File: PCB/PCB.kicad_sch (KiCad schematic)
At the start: 5 parts, among them J1 Ultrasonic Sensor, U1 Buck Converter Module, U2 Buck Converter Module, U3 ESP32-WROOM-32

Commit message: PCB Version
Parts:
- removed J1: Ultrasonic Sensor, Connector_PinHeader_2.54mm:PinHeader_1x04_P2.54mm_Vertical, symbol Connector:Conn_01x04_Socket
- U2: value Buck Converter Module -> Ultrasonic Sensor
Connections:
- net +5V: now reaches U2.1 (Pin_1)
- net Trig: now reaches U2.2 (Pin_2)
- net Trig: now also U3.26 (IO4)
- net Echo: now reaches U2.3 (Pin_3)
- net Echo: now also U3.29 (IO5)
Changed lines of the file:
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@@
+	(wire
+		(pts
+			(xy 106.68 66.04) (xy 104.14 66.04)
+		)
+		(stroke
+			(width 0)
+			(type default)
+		)
+	)
 	(wire
 		(pts
@@
 	(wire
 		(pts
-			(xy 157.48 62.23) (xy 162.56 62.23)
-		)
-		(stroke
-			(width 0)
-			(type default)
-		)
-	)
-	(wire
-		(pts
 			(xy 41.91 46.99) (xy 88.9 46.99)
 		)
@@
 	(wire
 		(pts
-			(xy 157.48 57.15) (xy 157.48 62.23)
-		)
-		(stroke
-			(width 0)
-			(type default)
-		)
-	)
-	(wire
-		(pts
 			(xy 20.32 82.55) (xy 41.91 82.55)
 		)
@@
 	(wire
 		(pts
-			(xy 160.02 59.69) (xy 162.56 59.69)
-		)
-		(stroke
-			(width 0)
-			(type default)
-		)
-	)
-	(wire
-		(pts
 			(xy 41.91 85.09) (xy 38.1 85.09)
 		)
@@
 	(wire
 		(pts
-			(xy 160.02 54.61) (xy 160.02 59.69)
+			(xy 123.19 64.77) (xy 123.19 58.42)
+		)
+		(stroke
+			(width 0)
+			(type default)
+		)
+	)
+	(wire
+		(pts
+			(xy 107.95 63.5) (xy 104.14 63.5)
+		)
+		(stroke
+			(width 0)
+			(type default)
+		)
+	)
+	(wire
+		(pts
+			(xy 125.73 67.31) (xy 107.95 67.31)
+		)
+		(stroke
+			(width 0)
+			(type default)
+		)
+	)
+	(wire
+		(pts
+			(xy 107.95 67.31) (xy 107.95 63.5)
 		)
 		(stroke
@@
 	(wire
 		(pts
-			(xy 142.24 54.61) (xy 160.02 54.61)
+			(xy 106.68 69.85) (xy 106.68 66.04)
+		)
+		(stroke
+			(width 0)
+			(type default)
+		)
+	)
+	(wire
+		(pts
+			(xy 125.73 64.77) (xy 123.19 64.77)
+		)
+		(stroke
+			(width 0)
+			(type default)
+		)
+	)
+	(wire
+		(pts
+			(xy 125.73 69.85) (xy 106.68 69.85)
 		)
 		(stroke
@@
 		)
 	)
-	(wire
-		(pts
-			(xy 142.24 57.15) (xy 157.48 57.15)
-		)
-		(stroke
-			(width 0)
-			(type default)
+	(label "Echo"
+		(at 118.11 69.85 0)
+		(effects
+			(font
+				(size 1.27 1.27)
+			)
+			(justify left bottom)
 		)
 	)
 	(label "3V3"
 		(at 85.09 46.99 0)
+		(effects
+			(font
+				(size 1.27 1.27)
+			)
+			(justify left bottom)
+		)
+	)
+	(label "Trig"
+		(at 118.11 67.31 0)
 		(effects
 			(font
@@
 	)
 	(symbol
+		(lib_id "power:+5V")
+		(at 123.19 58.42 0)
+		(unit 1)
+		(body_style 1)
+		(exclude_from_sim no)
+		(in_bom yes)
+		(on_board yes)
+		(in_pos_files yes)
+		(dnp no)
+		(fields_autoplaced yes)
+		(property "Reference" "#PWR05"
+			(at 123.19 62.23 0)
+			(hide yes)
+			(show_name no)
+			(do_not_autoplace no)
+			(effects
+				(font
+					(size 1.27 1.27)
+				)
+			)
+		)
+		(property "Value" "+5V"
+			(at 123.19 53.34 0)
+			(show_name no)
+			(do_not_autoplace no)
+			(effects
+				(font
+					(size 1.27 1.27)
+				)
+			)
+		)
+		(property "Footprint" ""
+			(at 123.19 58.42 0)
+			(hide yes)
+			(show_name no)
+			(do_not_autoplace no)
+			(effects
+				(font
+					(size 1.27 1.27)
+				)
+			)
+		)
+		(property "Datasheet" ""
+			(at 123.19 58.42 0)
+			(hide yes)
+			(show_name no)
+			(do_not_autoplace no)
+			(effects
+				(font
+					(size 1.27 1.27)
+				)
+			)
+		)
+		(property "Description" "Power symbol creates a global label with name \"+5V\""
+			(at 123.19 58.42 0)
+			(hide yes)
+			(show_name no)
+			(do_not_autoplace no)
+			(effects
+				(font
+					(size 1.27 1.27)
+				)
+			)
+		)
+		(pin "1"
+		)
+		(instances
+			(project "PCB"
+				(path "/ab40fc32-b885-4754-9572-45a5defa6a02"
+					(reference "#PWR05")
+					(unit 1)
+				)
+			)
+		)
+	)
+	(symbol
 		(lib_id "power:GND")
 		(at 88.9 119.38 0)
@@
 			)
 		)
-		(property "Value" "Buck Converter Module"
+		(property "Value" "Ultrasonic Sensor"
 			(at 133.35 69.8499 0)
 			(show_name no)
@@
 					(unit 1)
 				)
-			)
-		)
-	)
-	(symbol
-		(lib_id "Connector:Conn_01x04_Socket")
-		(at 167.64 59.69 0)
-		(unit 1)
-		(body_style 1)
-		(exclude_from_sim no)
-		(in_bom yes)
-		(on_board yes)
-		(in_pos_files yes)
-		(dnp no)
-		(property "Reference" "J1"
-			(at 171.958 61.976 0)
-			(hide yes)
-			(show_name no)
-			(do_not_autoplace no)
-			(effects
-				(font
-					(size 1.27 1.27)
-				)
-				(justify left)
-			)
-		)
-		(property "Value" "Ultrasonic Sensor"
-			(at 168.148 61.214 0)
-			(show_name no)
-			(do_not_autoplace no)
-			(effects
-				(font
-					(size 1.27 1.27)
-				)
-				(justify left)
-			)
-		)
-		(property "Footprint" "Connector_PinHeader_2.54mm:PinHeader_1x04_P2.54mm_Vertical"
-			(at 167.64 59.69 0)
-			(hide yes)
-			(show_name no)
-			(do_not_autoplace no)
-			(effects
-				(font
-					(size 1.27 1.27)
-				)
-			)
-		)
-		(property "Datasheet" ""
-			(at 167.64 59.69 0)
-			(hide yes)
-			(show_name no)
-			(do_not_autoplace no)
-			(effects
-				(font
-					(size 1.27 1.27)
-				)
-			)
-		)
-		(property "Description" "Generic connector, single row, 01x04, script generated"
-			(at 167.64 59.69 0)
-			(hide yes)
-			(show_name no)
-			(do_not_autoplace no)
-			(effects
-				(font
-					(size 1.27 1.27)
-				)
-			)
-		)
-		(pin "2"
-		)
-		(pin "4"
-		)
-		(pin "3"
-		)
-		(pin "1"
-		)
-		(instances
-			(project "PCB"
-				(path "/ab40fc32-b885-4754-9572-45a5defa6a02"
-					(reference "J1")
-					(unit 1)
-				)

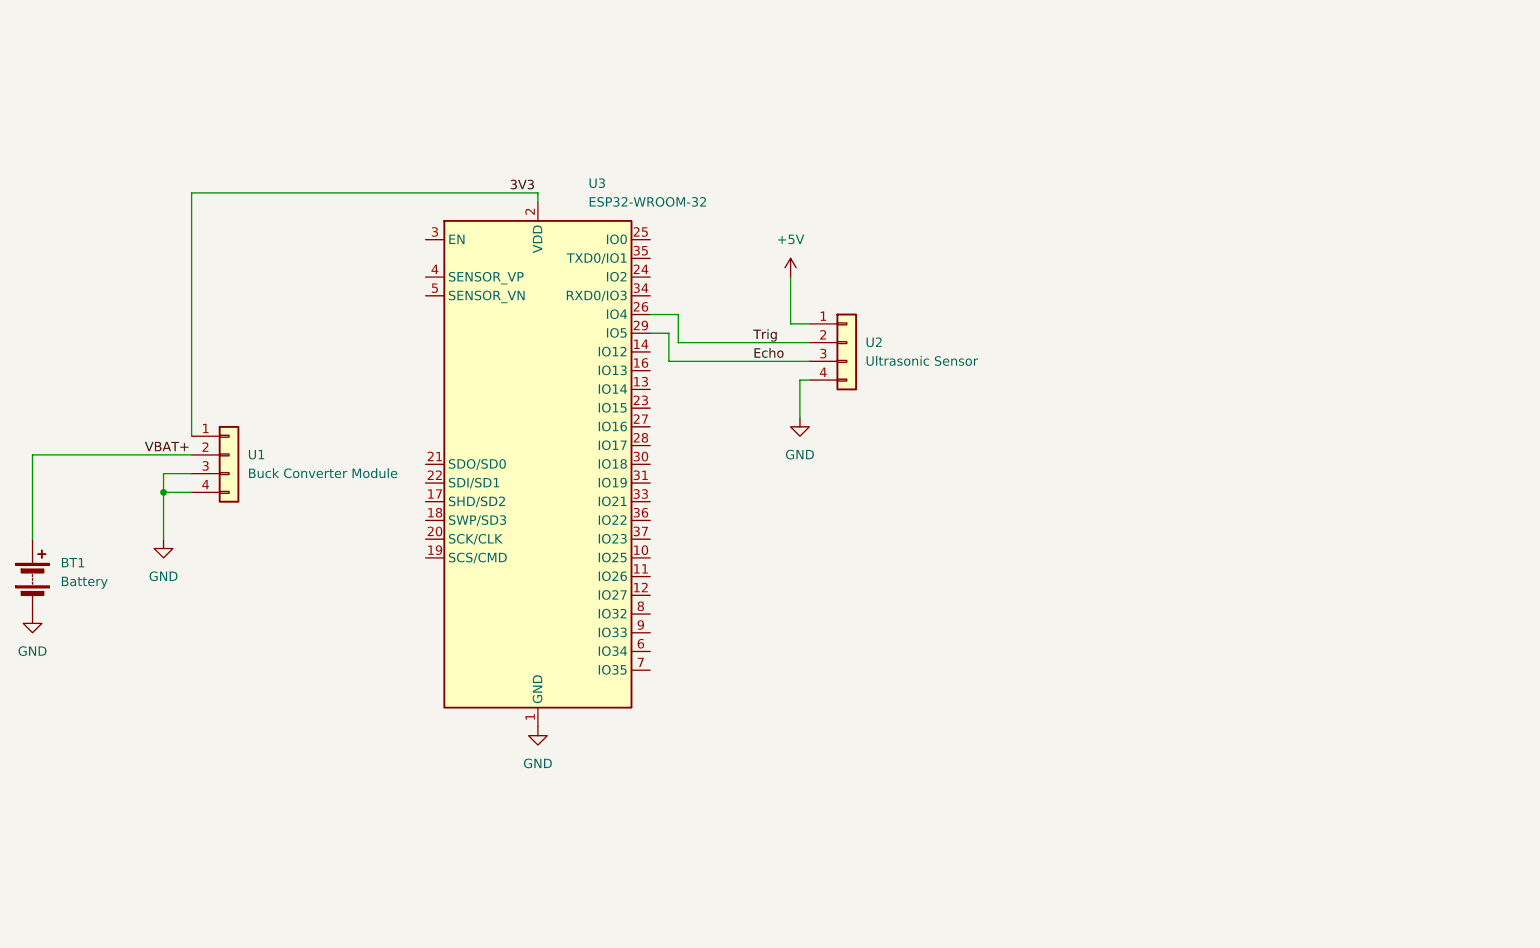
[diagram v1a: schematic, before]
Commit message: Update the PCB to support the new 4S batteyr charger, cleaned up the diagram, and added battery indicator support
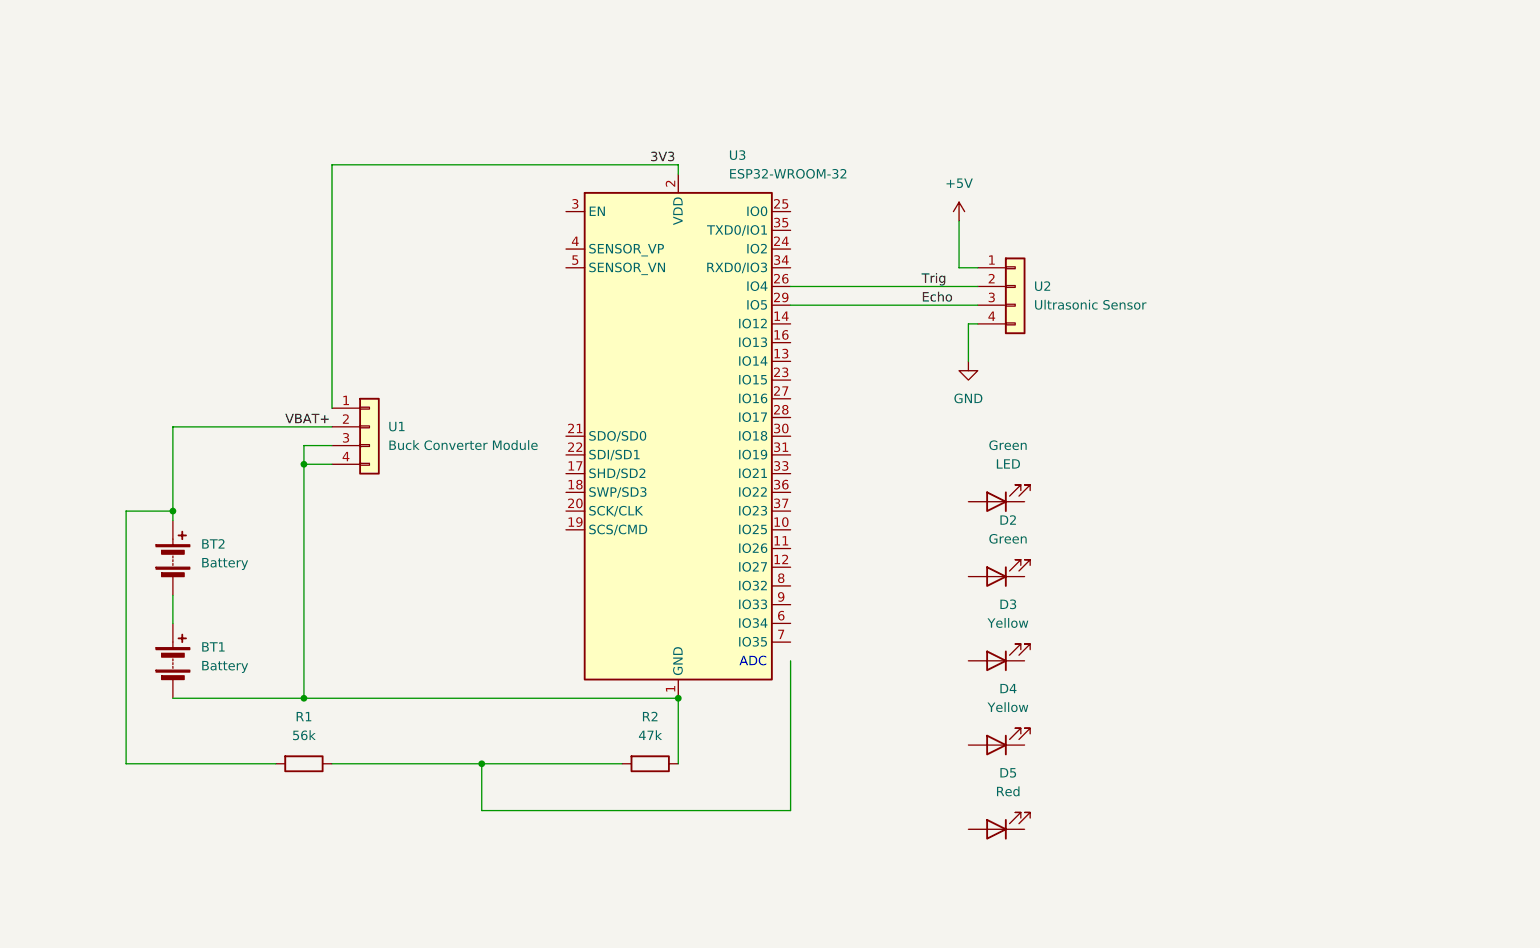
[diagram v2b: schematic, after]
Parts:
- added BT2: Battery, Battery:BatteryHolder_Keystone_2462_2xAA, symbol Device:Battery
- added D2: Green, symbol Device:LED
- added D3, D4: Yellow, symbol Device:LED
- added D5: Red, symbol Device:LED
- added Green: LED, symbol Device:LED
- added R1: 56k, symbol Device:R
- added R2: 47k, symbol Device:R
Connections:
- net GND: no longer BT1.2 (-), U1.3 (Pin_3), U1.4 (Pin_4), U3.1 (GND), U3.15 (GND), U3.38 (GND), U3.39 (GND)
- net VBAT+: now also BT2.1 (+), R1.2; no longer BT1.1 (+)
- new net: BT1.2 (-), R2.1, U1.3 (Pin_3), U1.4 (Pin_4), U3.1 (GND), U3.15 (GND), U3.38 (GND), U3.39 (GND)
- new net: BT1.1 (+), BT2.2 (-)
- new net: R1.1, R2.2
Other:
- note added: "ADC"
- moved on the sheet: BT1, U1, U2, U3

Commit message: Update PCB.kicad_sch
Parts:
- added J1: NiMH CHARGER CIRCUIT, symbol Connector_Generic:Conn_01x04
- U1: value Buck Converter Module -> Buck Converter
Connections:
- net ESP32-: now reaches R2.1, U1.3 (Pin_3), U1.4 (Pin_4), U3.1 (GND), U3.15 (GND), U3.38 (GND), U3.39 (GND)
- net ESP32-: now also D2.1 (K), D3.1 (K), D4.1 (K), D5.1 (K), Green.1 (K), J1.4 (Pin_4); no longer BT1.2 (-)
- net VBAT+ renamed 4SPACK+
- net 4SPACK+: now also J1.1 (Pin_1); no longer U1.2 (Pin_2)
- new net 4SPACK-: BT1.2 (-), J1.2 (Pin_2)
- new net OUT+: J1.3 (Pin_3), U1.2 (Pin_2)
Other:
- note added: "4S Battery"
- note added: "Battery Indicator"
- note added: "Battery V Detector"
- moved on the sheet: BT1, BT2, D2, D3, D4, D5, Green, R1, R2, U1, U2, U3

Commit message: Update PCB.kicad_sch
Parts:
- removed U3: ESP32-WROOM-32, RF_Module:ESP32-WROOM-32, symbol RF_Module:ESP32-WROOM-32
- added U4: Custom_ESP32_S3_Board, symbol ESP32_S3_Board:Custom_ESP32_S3_Board
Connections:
- net ESP32- is gone; now on net GND: D2.1 (K), D3.1 (K), D4.1 (K), D5.1 (K), Green.1 (K), J1.4 (Pin_4), R2.1, U1.3 (Pin_3), U1.4 (Pin_4)
- net GND: now also U4.25 (GND)
- net GPIO38: now reaches D2.2 (A)
- net GPIO38: now also U4.36 (GPIO38)
- net GPIO37: now reaches D3.2 (A)
- net GPIO37: now also U4.35 (GPIO37)
- net GPIO36: now reaches D4.2 (A)
- net GPIO36: now also U4.34 (GPIO36)
- net ADC: now reaches R1.1, R2.2
- net ADC: now also U4.4 (GPIO5)
- net GPIO35: now reaches D5.2 (A)
- net GPIO35: now also U4.33 (GPIO35)
- net GPIO39: now reaches Green.2 (A)
- net GPIO39: now also U4.37 (GPIO39)
- net 3V3: no longer names the net of U1.1 (Pin_1)
- net 3V3: now also U4.1 (3V3)
- net Echo renamed ECHO
- net ECHO: now also U4.18 (GPIO13)
- net Trig renamed TRIG
- net TRIG: now also U4.5 (GPIO6)
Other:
- note removed: "ADC"
- moved on the sheet: BT1, BT2, D2, D3, D4, D5, Green, J1, R1, R2, U1, U2

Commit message: PCB optimisation
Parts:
- D2, D3, D4, D5: footprint (none) -> LED_THT:LED_D5.0mm
- Green1: renamed from Green; footprint (none) -> LED_THT:LED_D5.0mm
- J1, U1, U2: footprint (none) -> Connector_PinHeader_2.54mm:PinHeader_1x04_P2.54mm_Vertical
- R1, R2: footprint (none) -> Resistor_THT:R_Axial_DIN0207_L6.3mm_D2.5mm_P7.62mm_Horizontal
- U4: footprint (none) -> Custom:ESP32-S3-DevKitC
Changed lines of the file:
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@@
 			)
 		)
-		(property "Footprint" ""
+		(property "Footprint" "Connector_PinHeader_2.54mm:PinHeader_1x04_P2.54mm_Vertical"
 			(at 85.09 49.53 0)
 			(hide yes)
@@
 			)
 		)
-		(property "Footprint" ""
+		(property "Footprint" "LED_THT:LED_D5.0mm"
 			(at 121.92 106.68 0)
 			(hide yes)
@@
 			)
 		)
-		(property "Footprint" ""
+		(property "Footprint" "LED_THT:LED_D5.0mm"
 			(at 121.92 118.11 0)
 			(hide yes)
@@
 			)
 		)
-		(property "Footprint" ""
+		(property "Footprint" "LED_THT:LED_D5.0mm"
 			(at 121.92 129.54 0)
 			(hide yes)
@@
 			)
 		)
-		(property "Footprint" ""
+		(property "Footprint" "Connector_PinHeader_2.54mm:PinHeader_1x04_P2.54mm_Vertical"
 			(at 82.55 130.81 0)
 			(hide yes)
@@
 			)
 		)
-		(property "Footprint" ""
+		(property "Footprint" "Custom:ESP32-S3-DevKitC"
 			(at 124.46 85.09 0)
 			(hide yes)
@@
 			)
 		)
-		(property "Footprint" ""
+		(property "Footprint" "Resistor_THT:R_Axial_DIN0207_L6.3mm_D2.5mm_P7.62mm_Horizontal"
 			(at 166.37 93.472 90)
 			(hide yes)
@@
 			)
 		)
-		(property "Footprint" ""
+		(property "Footprint" "Resistor_THT:R_Axial_DIN0207_L6.3mm_D2.5mm_P7.62mm_Horizontal"
 			(at 176.53 93.472 90)
 			(hide yes)
@@
 			)
 		)
-		(property "Footprint" ""
+		(property "Footprint" "LED_THT:LED_D5.0mm"
 			(at 121.92 140.97 0)
 			(hide yes)
@@
 		(dnp no)
 		(fields_autoplaced yes)
-		(property "Reference" "Green"
+		(property "Reference" "Green1"
 			(at 123.5075 88.9 0)
 			(show_name no)
@@
 			)
 		)
-		(property "Footprint" ""
+		(property "Footprint" "LED_THT:LED_D5.0mm"
 			(at 121.92 96.52 0)
 			(hide yes)
@@
 			(project "PCB"
 				(path "/ab40fc32-b885-4754-9572-45a5defa6a02"
-					(reference "Green")
+					(reference "Green1")
 					(unit 1)
 				)
@@
 			)
 		)
-		(property "Footprint" ""
+		(property "Footprint" "Connector_PinHeader_2.54mm:PinHeader_1x04_P2.54mm_Vertical"
 			(at 53.34 46.99 0)
 			(hide yes)

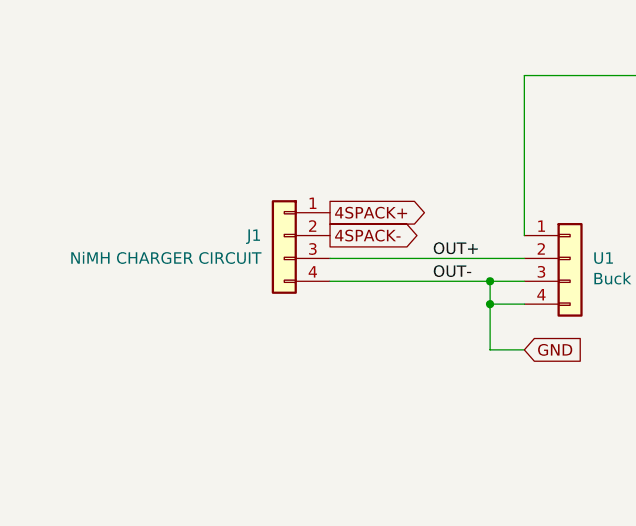
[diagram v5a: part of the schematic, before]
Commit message: removed unused component
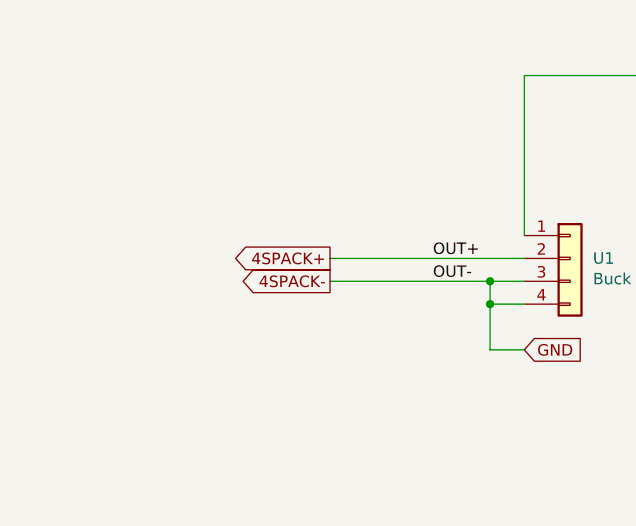
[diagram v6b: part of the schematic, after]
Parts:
- removed J1: NiMH CHARGER CIRCUIT, Connector_PinHeader_2.54mm:PinHeader_1x04_P2.54mm_Vertical, symbol Connector_Generic:Conn_01x04
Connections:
- net 4SPACK- is gone; now on net GND: BT1.2 (-)
- net OUT+ is gone; now on net 4SPACK+: U1.2 (Pin_2)
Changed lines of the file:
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@@
 	(global_label "4SPACK-"
 		(shape output)
-		(at 58.42 46.99 0)
-		(fields_autoplaced yes)
-		(effects
-			(font
-				(size 1.27 1.27)
-			)
-			(justify left)
-		)
-		(property "Intersheetrefs" "${INTERSHEET_REFS}"
-			(at 70.2952 46.99 0)
-			(hide yes)
-			(show_name no)
-			(do_not_autoplace no)
-			(effects
-				(font
-					(size 1.27 1.27)
-				)
-				(justify left)
+		(at 58.42 52.07 180)
+		(fields_autoplaced yes)
+		(effects
+			(font
+				(size 1.27 1.27)
+			)
+			(justify right)
+		)
+		(property "Intersheetrefs" "${INTERSHEET_REFS}"
+			(at 46.5448 52.07 0)
+			(hide yes)
+			(show_name no)
+			(do_not_autoplace no)
+			(effects
+				(font
+					(size 1.27 1.27)
+				)
+				(justify right)
 			)
 		)
@@
 	(global_label "4SPACK+"
 		(shape output)
-		(at 58.42 44.45 0)
-		(fields_autoplaced yes)
-		(effects
-			(font
-				(size 1.27 1.27)
-			)
-			(justify left)
-		)
-		(property "Intersheetrefs" "${INTERSHEET_REFS}"
-			(at 70.2952 44.45 0)
-			(hide yes)
-			(show_name no)
-			(do_not_autoplace no)
-			(effects
-				(font
-					(size 1.27 1.27)
-				)
-				(justify left)
+		(at 58.42 49.53 180)
+		(fields_autoplaced yes)
+		(effects
+			(font
+				(size 1.27 1.27)
+			)
+			(justify right)
+		)
+		(property "Intersheetrefs" "${INTERSHEET_REFS}"
+			(at 46.5448 49.53 0)
+			(hide yes)
+			(show_name no)
+			(do_not_autoplace no)
+			(effects
+				(font
+					(size 1.27 1.27)
+				)
+				(justify right)
 			)
 		)
@@
 					(unit 1)
 				)
-			)
-		)
-	)
-	(symbol
-		(lib_id "Connector_Generic:Conn_01x04")
-		(at 53.34 46.99 0)
-		(mirror y)
-		(unit 1)
-		(body_style 1)
-		(exclude_from_sim no)
-		(in_bom yes)
-		(on_board yes)
-		(in_pos_files yes)
-		(dnp no)
-		(property "Reference" "J1"
-			(at 50.8 46.9899 0)
-			(show_name no)
-			(do_not_autoplace no)
-			(effects
-				(font
-					(size 1.27 1.27)
-				)
-				(justify left)
-			)
-		)
-		(property "Value" "NiMH CHARGER CIRCUIT"
-			(at 50.8 49.5299 0)
-			(show_name no)
-			(do_not_autoplace no)
-			(effects
-				(font
-					(size 1.27 1.27)
-				)
-				(justify left)
-			)
-		)
-		(property "Footprint" "Connector_PinHeader_2.54mm:PinHeader_1x04_P2.54mm_Vertical"
-			(at 53.34 46.99 0)
-			(hide yes)
-			(show_name no)
-			(do_not_autoplace no)
-			(effects
-				(font
-					(size 1.27 1.27)
-				)
-			)
-		)
-		(property "Datasheet" ""
-			(at 53.34 46.99 0)
-			(hide yes)
-			(show_name no)
-			(do_not_autoplace no)
-			(effects
-				(font
-					(size 1.27 1.27)
-				)
-			)
-		)
-		(property "Description" "Generic connector, single row, 01x04, script generated (kicad-library-utils/schlib/autogen/connector/)"
-			(at 53.34 46.99 0)
-			(hide yes)
-			(show_name no)
-			(do_not_autoplace no)
-			(effects
-				(font
-					(size 1.27 1.27)
-				)
-			)
-		)
-		(pin "2"
-		)
-		(pin "1"
-		)
-		(pin "3"
-		)
-		(pin "4"
-		)
-		(instances
-			(project "PCB"
-				(path "/ab40fc32-b885-4754-9572-45a5defa6a02"
-					(reference "J1")
-					(unit 1)
-				)
